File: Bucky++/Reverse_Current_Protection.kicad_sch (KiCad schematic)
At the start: 36 parts, among them IC4 LTC4372CMS8#TRPBF, IC5 LTC4372CMS8#TRPBF, IC701 LTC4372CMS8#TRPBF, IC702 LTC4372CMS8#TRPBF, Q1 ISC016N04NM7V, Q2 ISC016N04NM7V, Q3 ISC016N04NM7V, Q4 ISC016N04NM7V, Q5 ISC016N04NM7V, Q6 ISC016N04NM7V, Q7 ISC016N04NM7V, Q8 ISC016N04NM7V

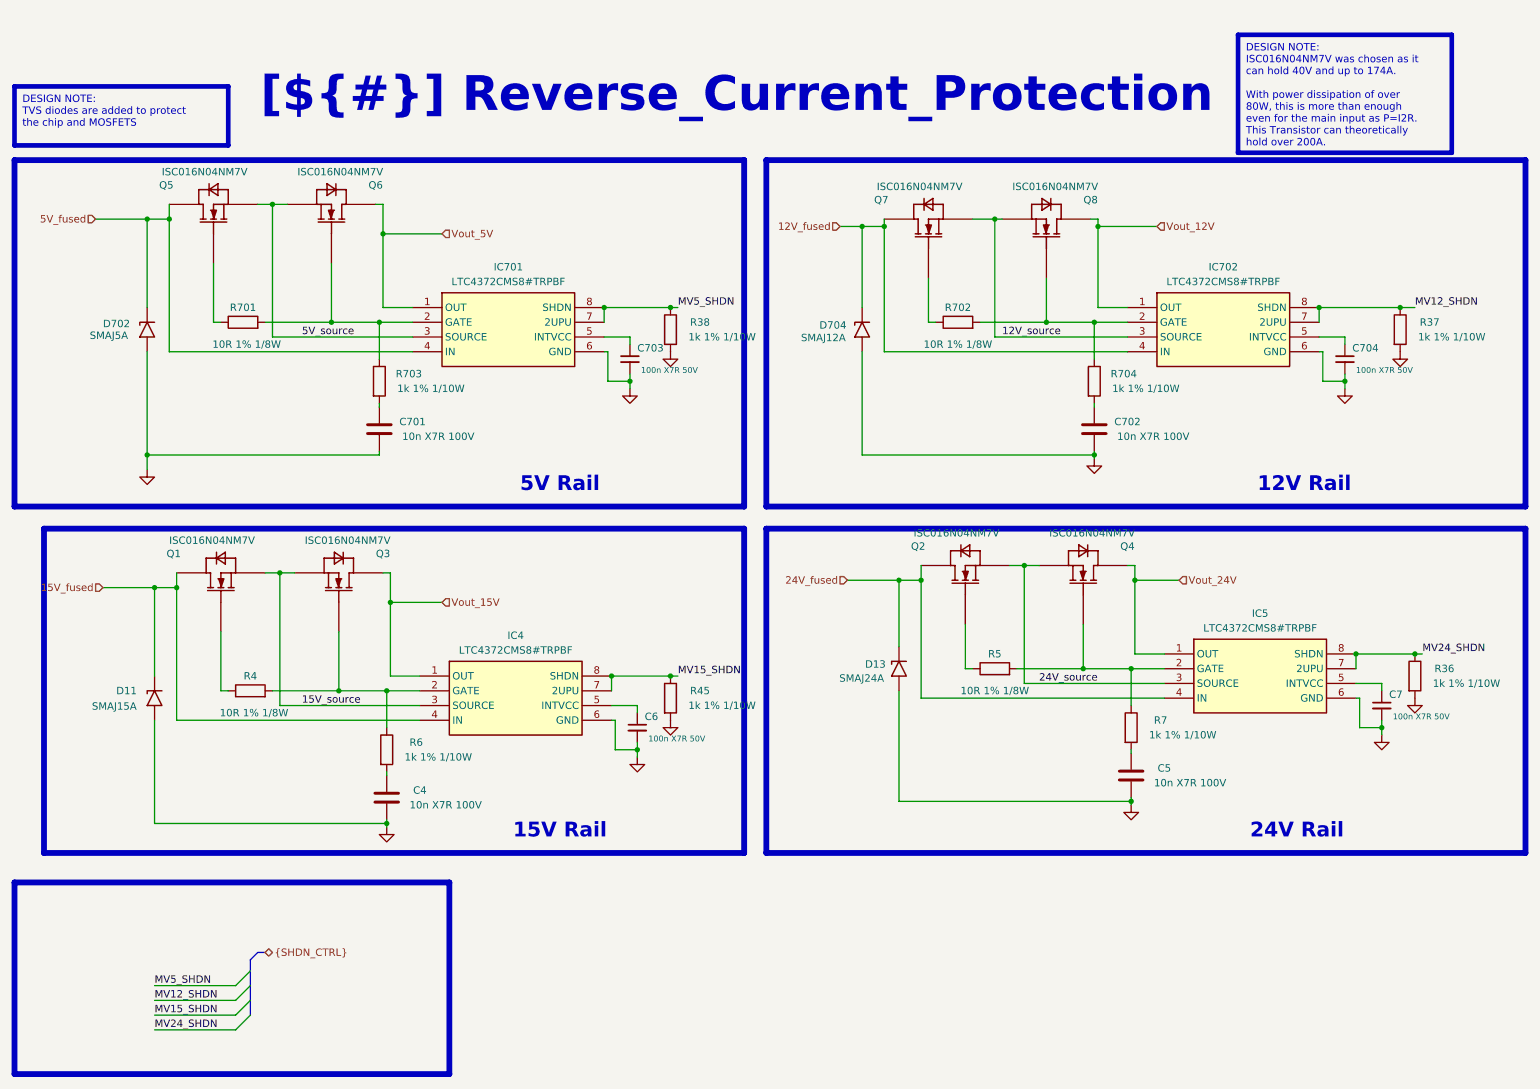
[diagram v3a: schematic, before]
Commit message: Cleared DRC errors, corrected routing errors, cleaned the schematic
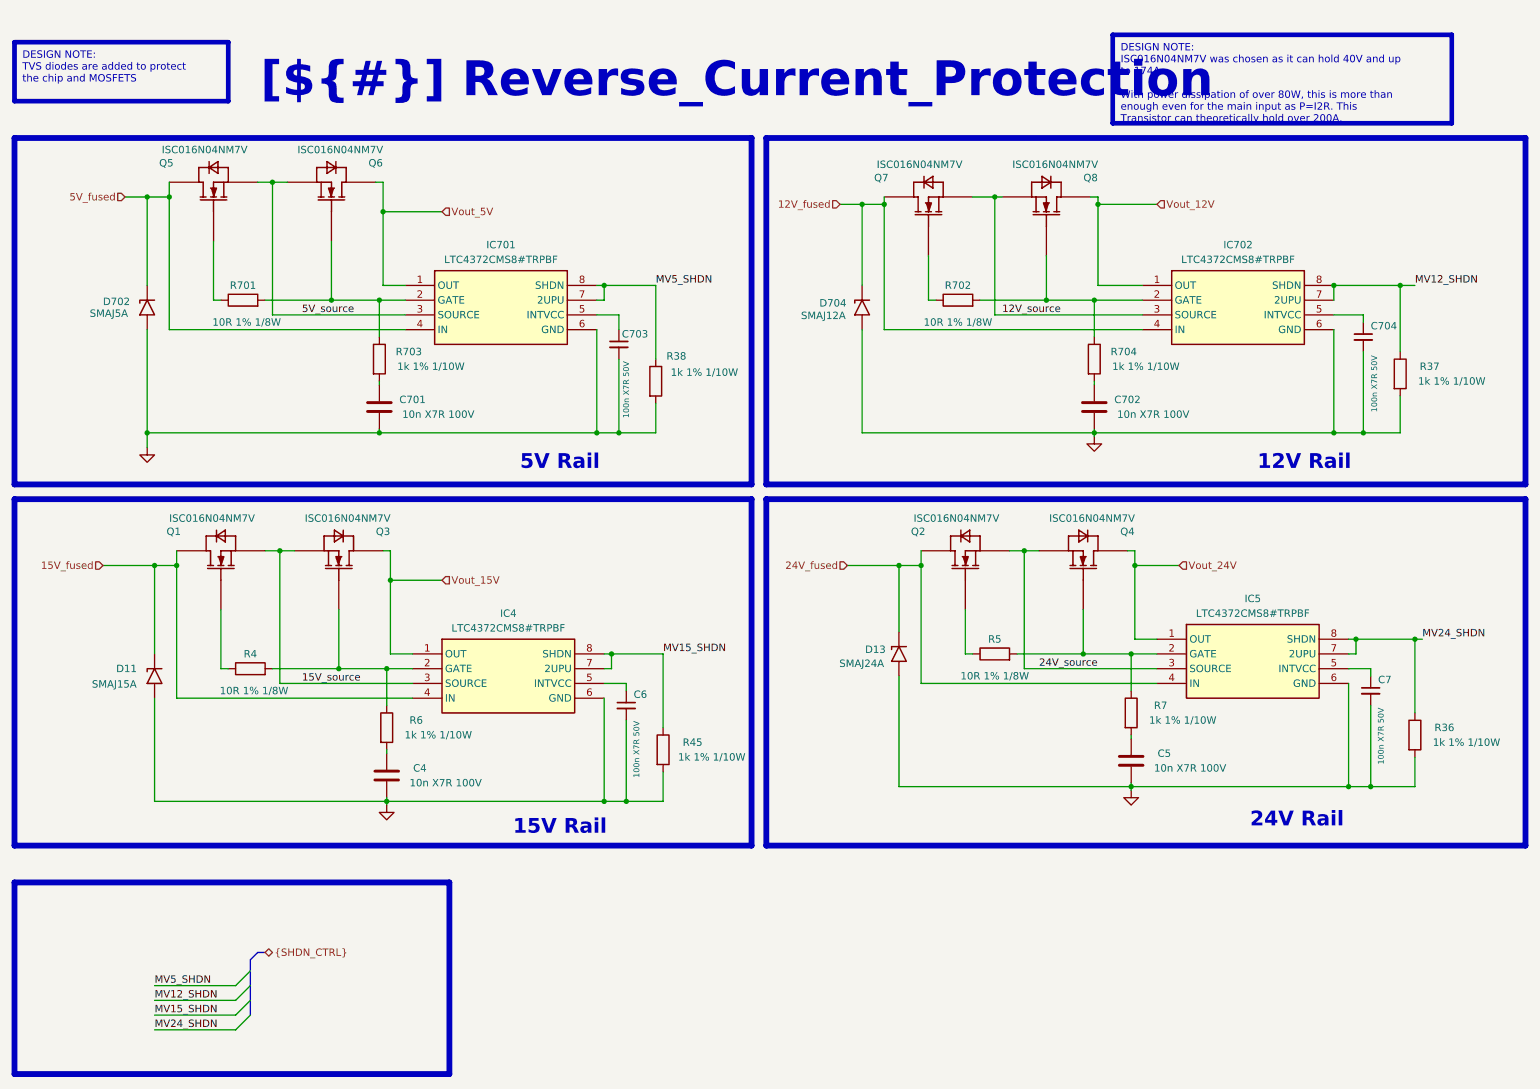
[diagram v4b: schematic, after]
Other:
- moved on the sheet: C4, C5, C6, C7, C701, C702, C703, C704, D11, D13, D702, D704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
